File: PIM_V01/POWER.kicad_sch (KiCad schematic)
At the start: 114 parts, among them J11 Conn_01x02, J12 Conn_01x02, J13 Conn_01x02, U10 TPS62933, U12 MP28167GQ-A-P, U6 TPS62933, U7 TPS62933, U8 TPS62933, U9 TPS62933

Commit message: updated some of the 3D bodies, and updated the BRINGUP plan with results from the first attempt at population; many components were not made in the order, so am now blocked waiting for those.
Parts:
- C101, C102, C43, C44, C45, C46, C47, C48, C59, C60, C61, C62, C76, C77: MPN (none) -> GRT188R61A226ME13D; PD (none) -> CAP CER 22UF 10V X5R 0603
- C28, C29, C30, C31, C32, C33, C49, C50, C51, C52: MPN (none) -> GRT188R61E106ME13D; PD (none) -> CAP CER 10UF 25V X5R 0603
- C34, C35, C36, C40, C41, C42, C53, C54, C57, C58, C70, C73, C74, C83, C84, C85, C86, C87, C88: MPN (none) -> GCM188R71H104KA57D; PD (none) -> CAP CER 0.1UF 50V X7R 0603
- C37, C39: MPN (none) -> AC0603KRX7R9BB333; PD (none) -> CAP CER 0.033UF 50V X7R 0603
- C38, C55, C56, C65, C66, C67: MPN (none) -> GCM188R71H103KA37J; PD (none) -> CAP CER 10000PF 50V X7R 0603
- C68, C75: MPN (none) -> GRT188R61E106ME13D; Note (none) -> 10uF for dev; PD (none) -> CAP CER 10UF 25V X5R 0603
- C69: value 22uF -> 22uF 25V; MPN (none) -> GRT188R61E106ME13D; PD (none) -> CAP CER 10UF 25V X5R 0603
- C71: MPN (none) -> GCM188R71H223KA37J; PD (none) -> CAP CER 0.022UF 50V X7R 0603
- C72: MPN (none) -> GCM188R71E105KA64J; PD (none) -> CAP CER 1UF 25V X7R 0603
- D10, D11, D12, D9: MPN XL-1608PGC-06 -> 150060GS75000; PD CHIP LED 0603 GREEN SMD -> LED GREEN CLEAR 0603 SMD
- J11, J12, J13: MPN (none) -> 61304011121; PD (none) -> CONN HEADER VERT 40POS 2.54MM
- L1, L2, L3, L4, L5: PD (none) -> FIXED IND 6.8UH 3.4A 60 MOHM SMD
- L6: PD (none) -> FIXED IND 4.7UH 5A 30.8 MOHM SMD
- R10, R22, R23, R24, R35, R36, R74, R75, R76, R77, R78, R9: MPN (none) -> ERJ-3GEY0R00V; PD (none) -> RES SMD 0 OHM JUMPER 1/10W 0603
- R25, R37: MPN (none) -> ERJ-3EKF5232V; PD (none) -> RES SMD 52.3K OHM 1% 1/10W 0603
- R26, R28, R30, R38, R40: MPN (none) -> ERJ-3EKF1002V; PD (none) -> RES SMD 10K OHM 1% 1/10W 0603
- R27, R39: MPN (none) -> ERJ-3EKF3162V; PD (none) -> RES SMD 31.6K OHM 1% 1/10W 0603
- R29: MPN (none) -> ERJ-3EKF4991V; PD (none) -> RES SMD 4.99K OHM 1% 1/10W 0603
- R31, R33: MPN (none) -> ERJ-3EKF4700V; PD (none) -> RES SMD 470 OHM 1% 1/10W 0603
- R32, R34: MPN (none) -> ERJ-3EKF1000V; PD (none) -> RES SMD 100 OHM 1% 1/10W 0603
- R45, R47, R49: MPN (none) -> ERJ-3EKF4703V; PD (none) -> RES SMD 470K OHM 1% 1/10W 0603
- R46, R48, R50, R71, R72, R73: MPN (none) -> ERJ-3EKF1003V; PD (none) -> RES SMD 100K OHM 1% 1/10W 0603
- R53: MPN (none) -> ERJ-3EKF4303V; PD (none) -> RES SMD 430K OHM 1% 1/10W 0603
- R54: MPN (none) -> ERJ-3EKF4023V; Note (none) -> 402k for dev; PD (none) -> RES SMD 402K OHM 1% 1/10W 0603
- R55: MPN (none) -> ERJ-3EKF2152V; PD (none) -> RES SMD 21.5K OHM 1% 1/10W 0603
- R56: MPN (none) -> ERJ-3EKF4322V; PD (none) -> RES SMD 43.2K OHM 1% 1/10W 0603
- U10, U6, U7, U8, U9: MPN (none) -> TPS62933DRLR; PD (none) -> IC REG BUCK ADJ 3A SOT583
- U12: footprint CustomFootprints:QFN-16_MP28167_MNP -> QFN-16_MP28167_MNP; PD (none) -> IC REG BUCK BOOST ADJ 3A 16QFN
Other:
- note added: "10UF FOR DEV"
- note added: "402 FOR DEV !!"
- note added: "PLACEHOLDER W 10UF FOR DEV"
- note added: "THESE MUST BE >>0603 FOR FLIGHT - RN ONLY RATED TO 10V"

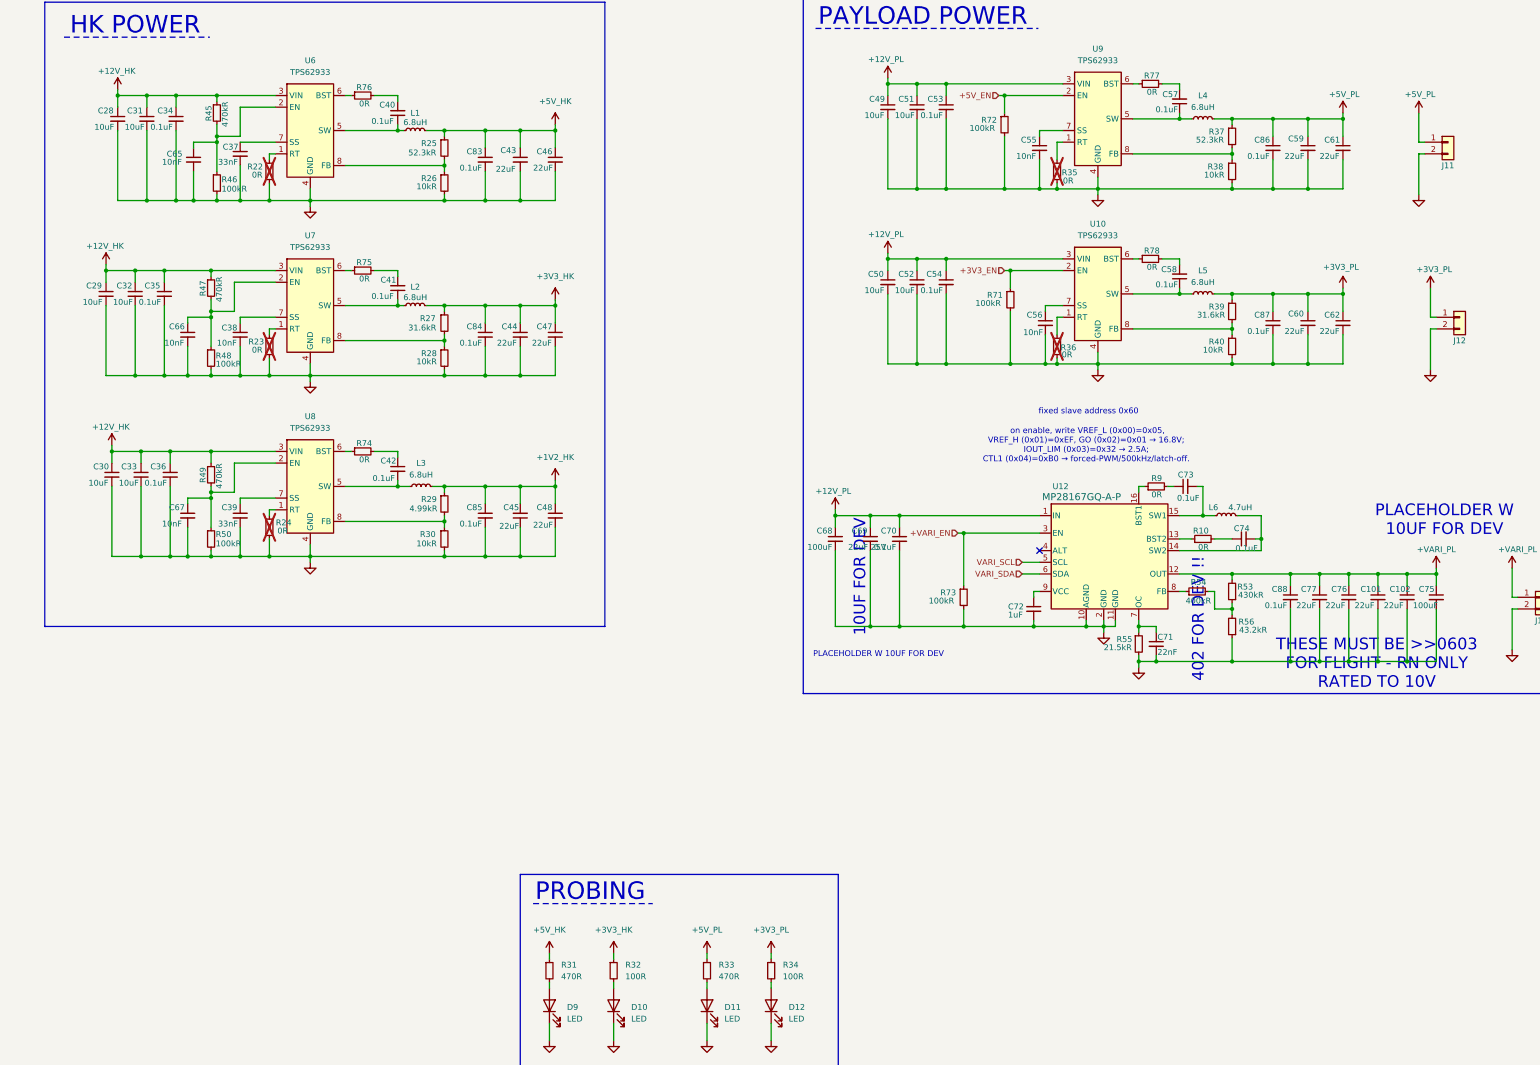
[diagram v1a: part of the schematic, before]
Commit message: finished uploading all of the correct footprints and 3D bodies. this is now done, and barely different than what was fabricated - used all manufacturers FPs (instead of kicads), but this didn't cause any of the original connections to break. I will now start on V02 (incl FPGA and smaller)
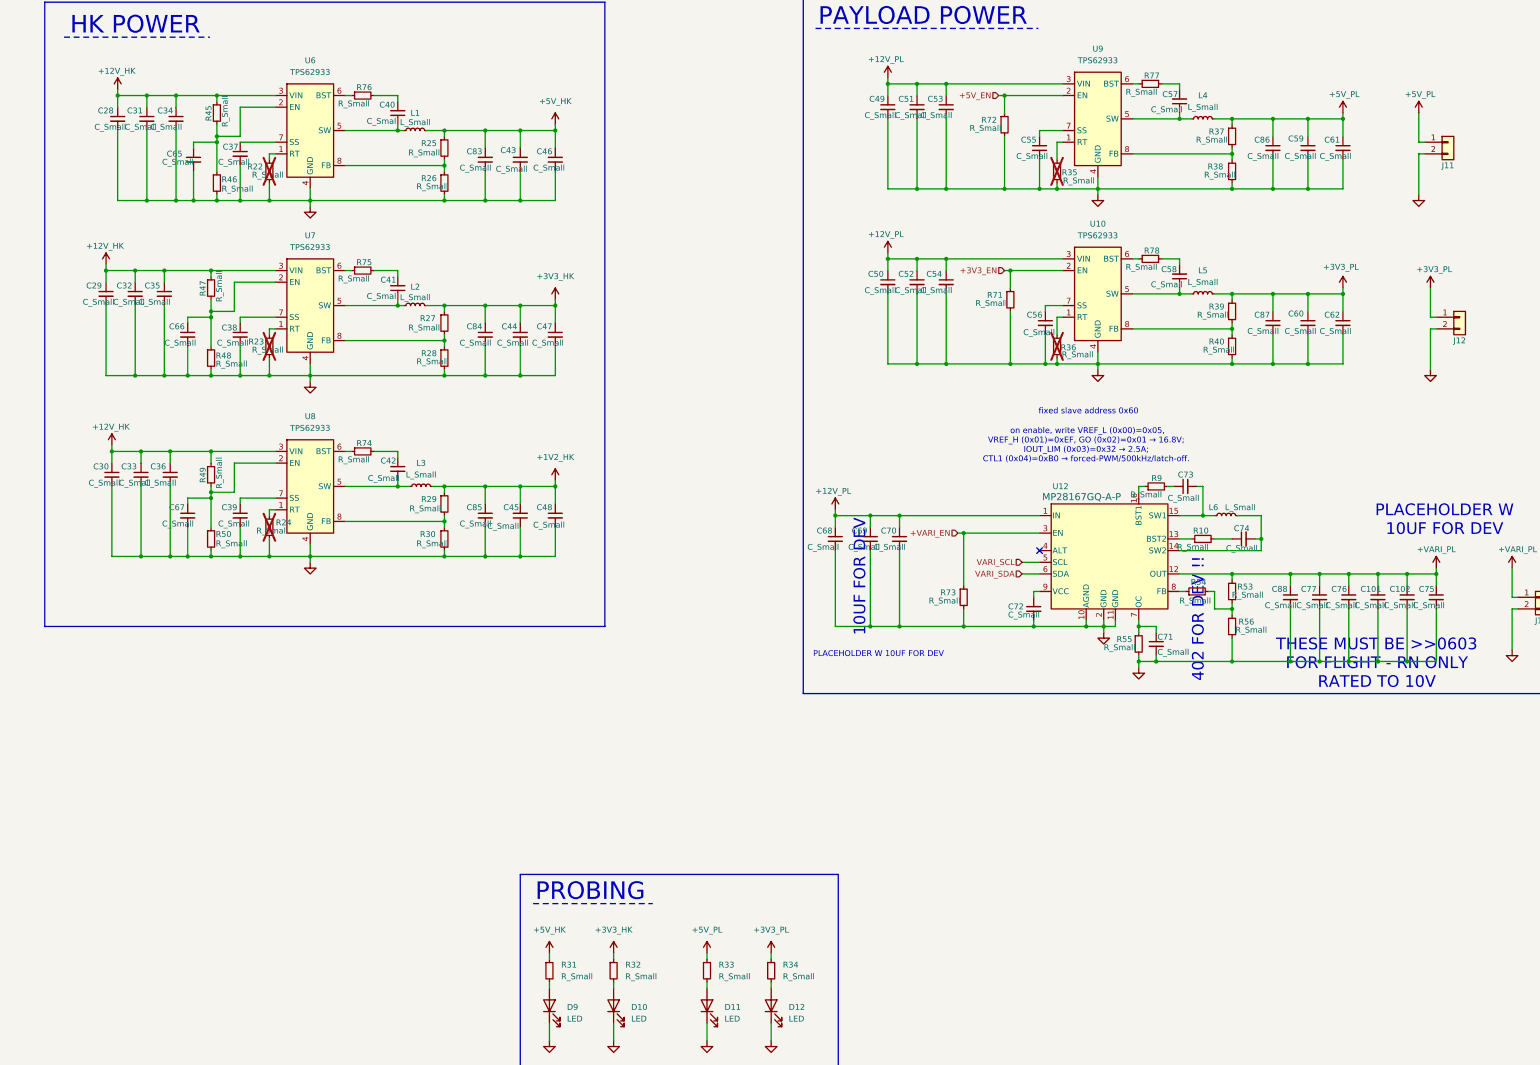
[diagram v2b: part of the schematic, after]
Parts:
- C101, C102, C43, C44, C45, C46, C47, C48, C59, C60, C61, C62, C76, C77: value 22uF -> C_Small
- C28, C29, C30, C31, C32, C33, C49, C50, C51, C52: value 10uF -> C_Small
- C34, C35, C36, C40, C41, C42, C53, C54, C57, C58, C70, C73, C74, C83, C84, C85, C86, C87, C88: value 0.1uF -> C_Small
- C37, C39: value 33nF -> C_Small
- C38, C55, C56, C65, C66, C67: value 10nF -> C_Small
- C68, C75: value 100uF -> C_Small
- C69: value 22uF 25V -> C_Small
- C71: value 22nF -> C_Small
- C72: value 1uF -> C_Small
- L1, L2, L3, L4, L5: value 6.8uH -> L_Small
- L6: value 4.7uH -> L_Small
- R10, R22, R23, R24, R35, R36, R74, R75, R76, R77, R78, R9: value 0R -> R_Small
- R25, R37: value 52.3kR -> R_Small
- R26, R28, R30, R38, R40: value 10kR -> R_Small
- R27, R39: value 31.6kR -> R_Small
- R29: value 4.99kR -> R_Small
- R31, R33: value 470R -> R_Small
- R32, R34: value 100R -> R_Small
- R45, R47, R49: value 470kR -> R_Small
- R46, R48, R50, R71, R72, R73: value 100kR -> R_Small
- R53: value 430kR -> R_Small
- R54: value 400kR -> R_Small
- R55: value 21.5kR -> R_Small
- R56: value 43.2kR -> R_Small
- U12: footprint QFN-16_MP28167_MNP -> CustomFootprints:MP28167GQ-A-P

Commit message: somehow last push my components had lost their values, and only displayed their Kicad value, but I fixed that now
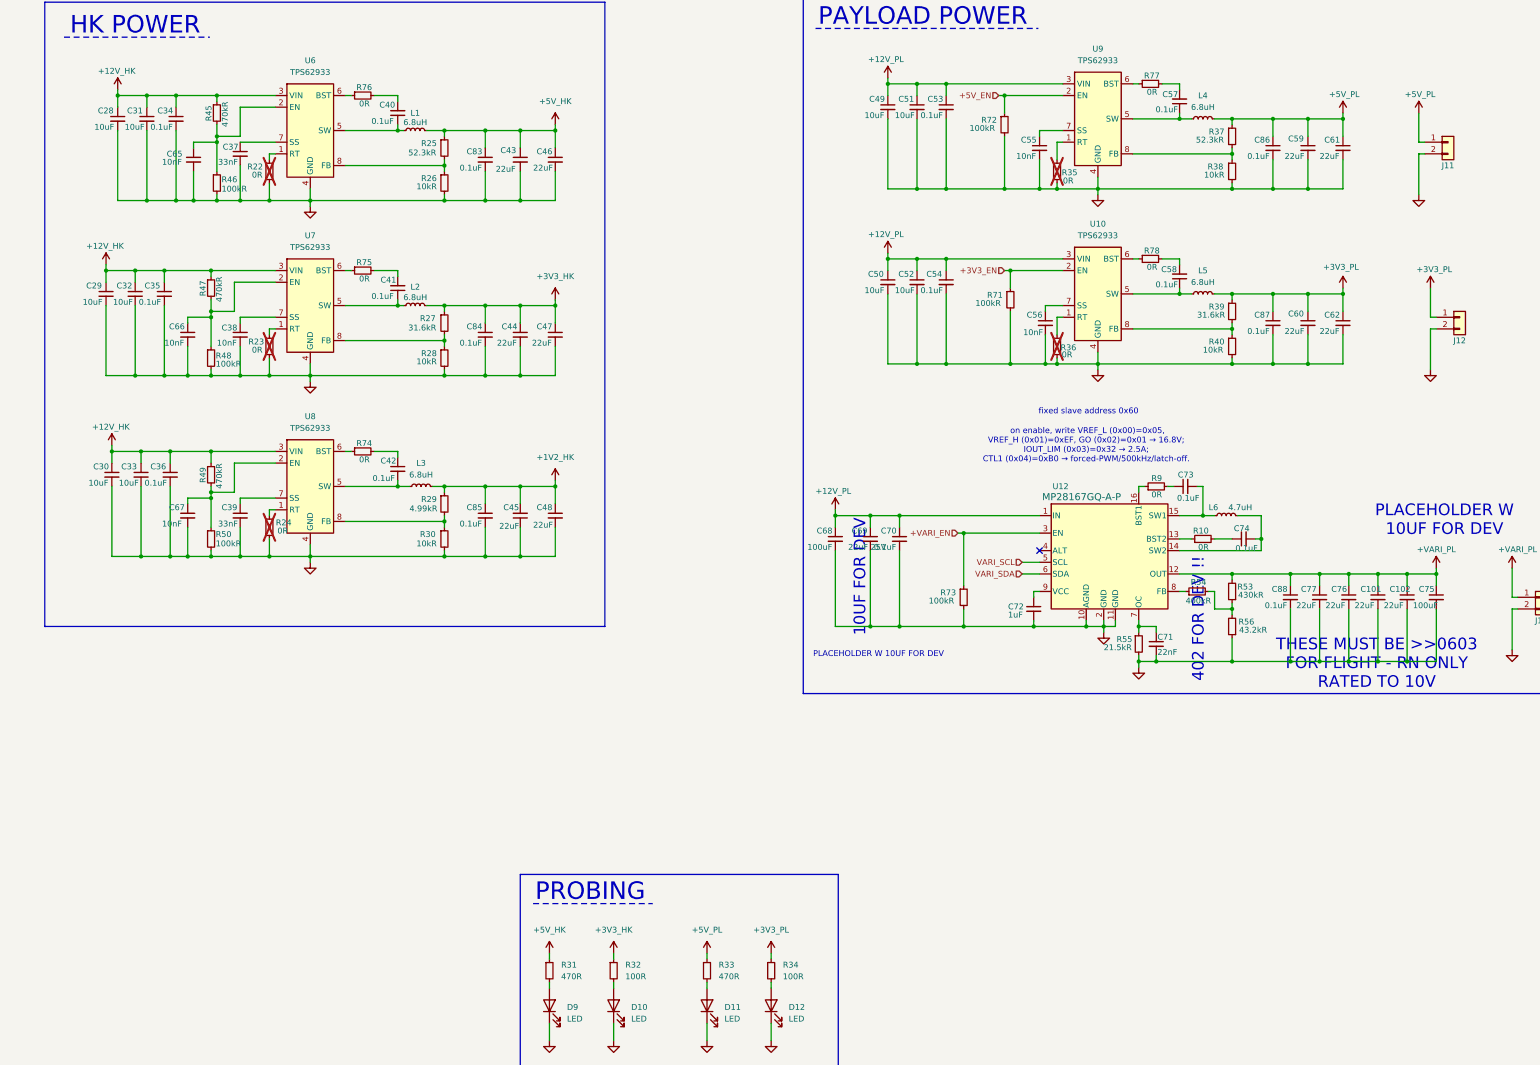
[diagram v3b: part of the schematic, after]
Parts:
- C101, C102, C43, C44, C45, C46, C47, C48, C59, C60, C61, C62, C76, C77: value C_Small -> 22uF
- C28, C29, C30, C31, C32, C33, C49, C50, C51, C52: value C_Small -> 10uF
- C34, C35, C36, C40, C41, C42, C53, C54, C57, C58, C70, C73, C74, C83, C84, C85, C86, C87, C88: value C_Small -> 0.1uF
- C37, C39: value C_Small -> 33nF
- C38, C55, C56, C65, C66, C67: value C_Small -> 10nF
- C68, C75: value C_Small -> 100uF
- C69: value C_Small -> 22uF 25V
- C71: value C_Small -> 22nF
- C72: value C_Small -> 1uF
- L1, L2, L3, L4, L5: value L_Small -> 6.8uH
- L6: value L_Small -> 4.7uH
- R10, R22, R23, R24, R35, R36, R74, R75, R76, R77, R78, R9: value R_Small -> 0R
- R25, R37: value R_Small -> 52.3kR
- R26, R28, R30, R38, R40: value R_Small -> 10kR
- R27, R39: value R_Small -> 31.6kR
- R29: value R_Small -> 4.99kR
- R31, R33: value R_Small -> 470R
- R32, R34: value R_Small -> 100R
- R45, R47, R49: value R_Small -> 470kR
- R46, R48, R50, R71, R72, R73: value R_Small -> 100kR
- R53: value R_Small -> 430kR
- R54: value R_Small -> 400kR
- R55: value R_Small -> 21.5kR
- R56: value R_Small -> 43.2kR
- U12: footprint CustomFootprints:MP28167GQ-A-P -> QFN-16_MP28167_MNP

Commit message: updated the last few component symbols/fps, none very significant
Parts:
- U12: footprint QFN-16_MP28167_MNP -> CustomFootprints:MP28167GQ-A-P
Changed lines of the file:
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@@
 			)
 		)
-		(property "Footprint" "QFN-16_MP28167_MNP"
+		(property "Footprint" "CustomFootprints:MP28167GQ-A-P"
 			(at 250.698 168.656 0)
 			(effects
